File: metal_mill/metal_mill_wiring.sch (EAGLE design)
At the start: 15 parts

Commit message: First fully documented commit. Some details like the FCCH_RFID_ESTOP board layout still need to be done.
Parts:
- added U$9: AC_JACK, fcch_eagle_parts_metal_mill:AC_JACK
- added X_AXIS1: GX16-8, fcch_eagle_parts_metal_mill:GX16-8
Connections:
- removed net N$16: U$1.INPUT9, U$5.T-ALARM
- removed net N$40: U$3.CHANNEL_B, U$8.P$6
- new net +12V: U$5.+12V-AUX, U$6.IN+, X_AXIS1.T3
- new net N$24: U$4.CHANNEL_B, X_AXIS.T7
- new net N$34: U$2.CHANNEL_A, U$7.T6
- new net N$46: U$1.INPUT2, XMIN.3
- new net N$47: U$1.INPUT3, XMAX.3
- new net N$48: U$1.INPUT4, YMIN.3
- new net N$49: U$1.INPUT5, YMAX.3
- new net N$50: U$1.INPUT6, ZMIN.3
- new net N$51: U$1.INPUT7, ZMAX.3
- new net N$52: X_AXIS1.T5
- net GND: now also U$1.GND_IN, U$5.GND-AUX, U$6.IN-, U$6.OUT_GND, U$7.T8, U$8.T8, X_AXIS.T8, X_AXIS1.T1; no longer U$7.P$7, U$8.P$7, X_AXIS.P$7
- net N$12: now also U$5.FGND, U$9.GROUND; no longer U$5.+12V-AUX, U$6.IN+
- net N$13: now also U$7.T1; no longer U$7.P$1
- net N$14: now also U$1.INPUT0; no longer U$1.INPUT10
- net N$15: now also U$5.AC/N, U$9.NUETRAL; no longer U$1.+5V_IN, U$1.IN_COM, U$1.OUT0+, U$1.OUT1+, U$1.OUT2+, U$1.OUT3+, U$6.+5V
- net N$17: now also U$7.T2; no longer U$7.P$2
- net N$18: now also U$3.CHANNEL_B, U$8.T7; no longer U$2.ENC_GND, U$7.P$3
- net N$19: now also U$1.OUT1-, U$5.ON/OFF; no longer U$1.INPUT0, XMAX.3
- net N$20: now also U$5.AC/L, U$9.LINE; no longer U$1.GND_IN, U$5.GND-AUX, U$6.GND, U$6.IN-
- net N$21: now also U$1.INPUT8, X_AXIS1.T4; no longer U$1.INPUT6, U$1.OUT0-
- net N$22: now also U$1.INPUT9; no longer U$1.INPUT7, U$1.OUT1-
- net N$23: now also U$1.INPUT10, X_AXIS1.T6; no longer U$1.INPUT8, U$1.OUT2-
- net N$25: now also U$3.CHANNEL_A, U$8.T6; no longer U$2.ENC_5VDC, U$7.P$4
- net N$26: now also U$3.ENC_5VDC, U$8.T5; no longer U$2.CHANNEL_A, U$7.P$5
- net N$27: now also U$3.ENC_GND, U$8.T4; no longer U$2.CHANNEL_B, U$7.P$6
- net N$28: now also X_AXIS.T1; no longer X_AXIS.P$1
- net N$29: now also X_AXIS.T2; no longer X_AXIS.P$2
- net N$30: now also U$4.CHANNEL_A, X_AXIS.T6; no longer U$4.ENC_GND, X_AXIS.P$3
- net N$31: now also X_AXIS.T5; no longer X_AXIS.P$4
- net N$32: now also U$4.ENC_GND, X_AXIS.T4; no longer U$4.CHANNEL_A, X_AXIS.P$5
- net N$33: now also U$2.CHANNEL_B, U$7.T7; no longer U$4.CHANNEL_B, X_AXIS.P$6
- net N$35: now also U$8.T1; no longer U$8.P$1
- net N$36: now also U$8.T2; no longer U$8.P$2
- net N$37: now also U$2.ENC_5VDC, U$7.T5; no longer U$3.ENC_GND, U$8.P$3
- net N$38: now also U$2.ENC_GND, U$7.T4; no longer U$3.ENC_5VDC, U$8.P$4
- net N$39: now also U$1.+5V_IN, U$6.OUT_+5V, X_AXIS1.T2; no longer U$3.CHANNEL_A, U$8.P$5
- net N$41: now also U$1.OUT1+, U$5.+5V-AUX; no longer U$1.INPUT1, XMIN.3
- net N$42: now also U$1.OUT0-, X_AXIS1.T7; no longer U$1.INPUT2, YMIN.3
- net N$43: now also U$1.INPUT1, U$5.T-ALARM; no longer U$1.INPUT3, YMAX.3
- net N$44: now also U$1.OUT0+, X_AXIS1.T8; no longer U$1.INPUT4, ZMIN.3
- net N$45: now also U$1.IN_COM; no longer U$1.INPUT5, ZMAX.3
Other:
- note added: "A/C Power In"
- note added: "E-Stop and RFID Module"
- note added: "W1"
- note added: "W2"
- note added: "W3"
- note added: "W4"
- note added: "W5"
- note added: "W6"
- note added: "W7"
- note added: "W9"
- note added: "X Axis Pwr and Enc"
- note added: "Y Axis Pwr and Enc"
- note added: "Z Axis Pwr and Enc"
- moved on the sheet: XMAX, XMIN, YMAX, YMIN, ZMAX, ZMIN

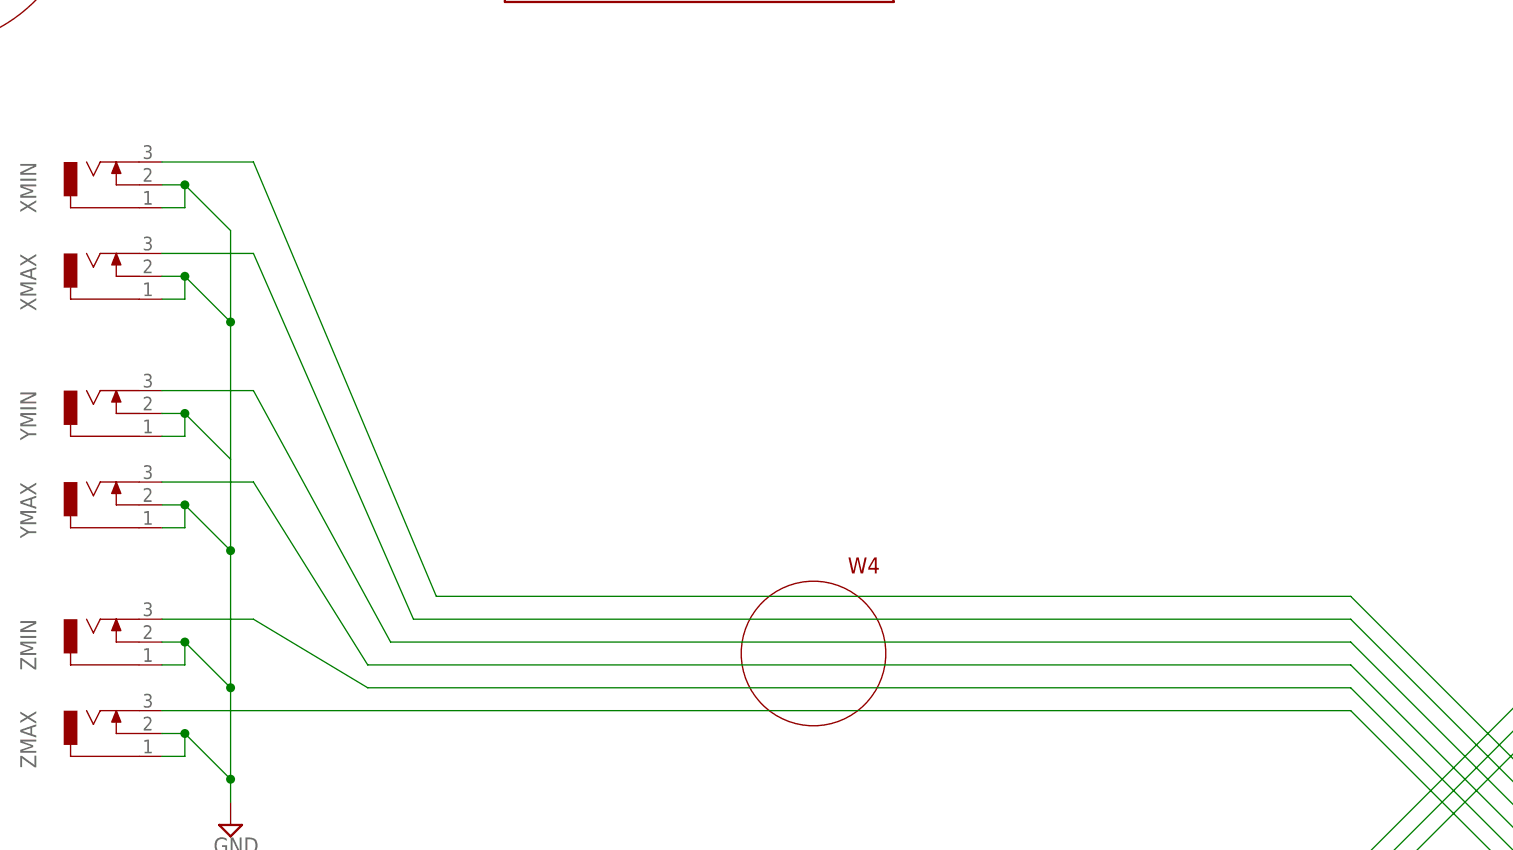
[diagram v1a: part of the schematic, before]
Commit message: fixed some mistakes found by prototyping on a breadboard. * moved wire terminals to the end of the board * updated LED devices (was using a header) * updated resistor values
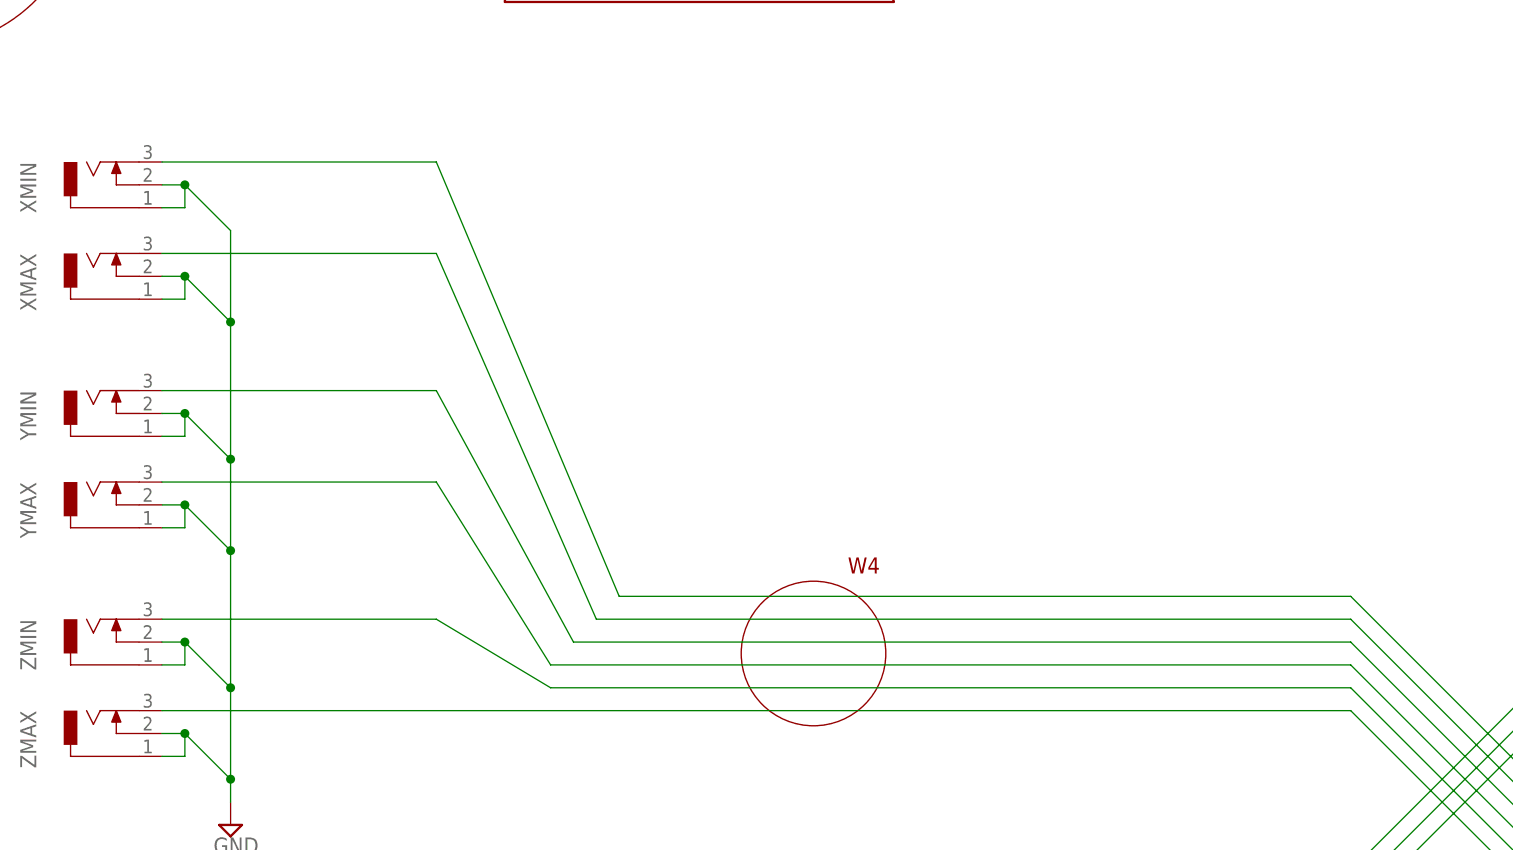
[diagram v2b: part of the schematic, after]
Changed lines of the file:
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@@
 <junction x="-137.16" y="198.12"/>
 <junction x="-132.08" y="182.88"/>
+<junction x="-132.08" y="167.64"/>
 </segment>
 <segment>
@@
 <segment>
 <pinref part="XMIN" gate="G$1" pin="3"/>
-<wire x1="-109.22" y1="152.4" x2="-129.54" y2="200.66" width="0.1524" layer="91"/>
-<wire x1="-129.54" y1="200.66" x2="-139.7" y2="200.66" width="0.1524" layer="91"/>
+<wire x1="-88.9" y1="152.4" x2="-109.22" y2="200.66" width="0.1524" layer="91"/>
 <pinref part="U$1" gate="G$1" pin="INPUT2"/>
+<wire x1="-109.22" y1="200.66" x2="-139.7" y2="200.66" width="0.1524" layer="91"/>
 <wire x1="71.12" y1="88.9" x2="55.88" y2="88.9" width="0.1524" layer="91"/>
 <wire x1="55.88" y1="88.9" x2="-7.62" y2="152.4" width="0.1524" layer="91"/>
-<wire x1="-7.62" y1="152.4" x2="-109.22" y2="152.4" width="0.1524" layer="91"/>
+<wire x1="-7.62" y1="152.4" x2="-88.9" y2="152.4" width="0.1524" layer="91"/>
 </segment>
 </net>
@@
 <segment>
 <pinref part="XMAX" gate="G$1" pin="3"/>
-<wire x1="-111.76" y1="149.86" x2="-129.54" y2="190.5" width="0.1524" layer="91"/>
-<wire x1="-129.54" y1="190.5" x2="-139.7" y2="190.5" width="0.1524" layer="91"/>
+<wire x1="-91.44" y1="149.86" x2="-109.22" y2="190.5" width="0.1524" layer="91"/>
 <pinref part="U$1" gate="G$1" pin="INPUT3"/>
+<wire x1="-109.22" y1="190.5" x2="-139.7" y2="190.5" width="0.1524" layer="91"/>
 <wire x1="71.12" y1="86.36" x2="55.88" y2="86.36" width="0.1524" layer="91"/>
 <wire x1="55.88" y1="86.36" x2="-7.62" y2="149.86" width="0.1524" layer="91"/>
-<wire x1="-7.62" y1="149.86" x2="-111.76" y2="149.86" width="0.1524" layer="91"/>
+<wire x1="-7.62" y1="149.86" x2="-91.44" y2="149.86" width="0.1524" layer="91"/>
 </segment>
 </net>
@@
 <segment>
 <pinref part="YMIN" gate="G$1" pin="3"/>
-<wire x1="-114.3" y1="147.32" x2="-129.54" y2="175.26" width="0.1524" layer="91"/>
-<wire x1="-129.54" y1="175.26" x2="-139.7" y2="175.26" width="0.1524" layer="91"/>
+<wire x1="-93.98" y1="147.32" x2="-109.22" y2="175.26" width="0.1524" layer="91"/>
 <pinref part="U$1" gate="G$1" pin="INPUT4"/>
+<wire x1="-109.22" y1="175.26" x2="-139.7" y2="175.26" width="0.1524" layer="91"/>
 <wire x1="71.12" y1="83.82" x2="55.88" y2="83.82" width="0.1524" layer="91"/>
 <wire x1="55.88" y1="83.82" x2="-7.62" y2="147.32" width="0.1524" layer="91"/>
-<wire x1="-7.62" y1="147.32" x2="-114.3" y2="147.32" width="0.1524" layer="91"/>
+<wire x1="-7.62" y1="147.32" x2="-93.98" y2="147.32" width="0.1524" layer="91"/>
 </segment>
 </net>
@@
 <segment>
 <pinref part="YMAX" gate="G$1" pin="3"/>
-<wire x1="-116.84" y1="144.78" x2="-129.54" y2="165.1" width="0.1524" layer="91"/>
-<wire x1="-129.54" y1="165.1" x2="-139.7" y2="165.1" width="0.1524" layer="91"/>
+<wire x1="-96.52" y1="144.78" x2="-109.22" y2="165.1" width="0.1524" layer="91"/>
 <pinref part="U$1" gate="G$1" pin="INPUT5"/>
+<wire x1="-109.22" y1="165.1" x2="-139.7" y2="165.1" width="0.1524" layer="91"/>
 <wire x1="71.12" y1="81.28" x2="55.88" y2="81.28" width="0.1524" layer="91"/>
 <wire x1="55.88" y1="81.28" x2="-7.62" y2="144.78" width="0.1524" layer="91"/>
-<wire x1="-7.62" y1="144.78" x2="-116.84" y2="144.78" width="0.1524" layer="91"/>
+<wire x1="-7.62" y1="144.78" x2="-96.52" y2="144.78" width="0.1524" layer="91"/>
 </segment>
 </net>
@@
 <segment>
 <pinref part="ZMIN" gate="G$1" pin="3"/>
-<wire x1="-116.84" y1="142.24" x2="-129.54" y2="149.86" width="0.1524" layer="91"/>
-<wire x1="-129.54" y1="149.86" x2="-139.7" y2="149.86" width="0.1524" layer="91"/>
+<wire x1="-96.52" y1="142.24" x2="-109.22" y2="149.86" width="0.1524" layer="91"/>
 <pinref part="U$1" gate="G$1" pin="INPUT6"/>
+<wire x1="-109.22" y1="149.86" x2="-139.7" y2="149.86" width="0.1524" layer="91"/>
 <wire x1="71.12" y1="78.74" x2="55.88" y2="78.74" width="0.1524" layer="91"/>
 <wire x1="55.88" y1="78.74" x2="-7.62" y2="142.24" width="0.1524" layer="91"/>
-<wire x1="-7.62" y1="142.24" x2="-116.84" y2="142.24" width="0.1524" layer="91"/>
-</segment>
-</net>
+<wire x1="-7.62" y1="142.24" x2="-96.52" y2="142.24" width="0.1524" layer="91"/>
+</segment>
+</net>
